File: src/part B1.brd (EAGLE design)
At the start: 41 x 75.5 mm, 0 parts

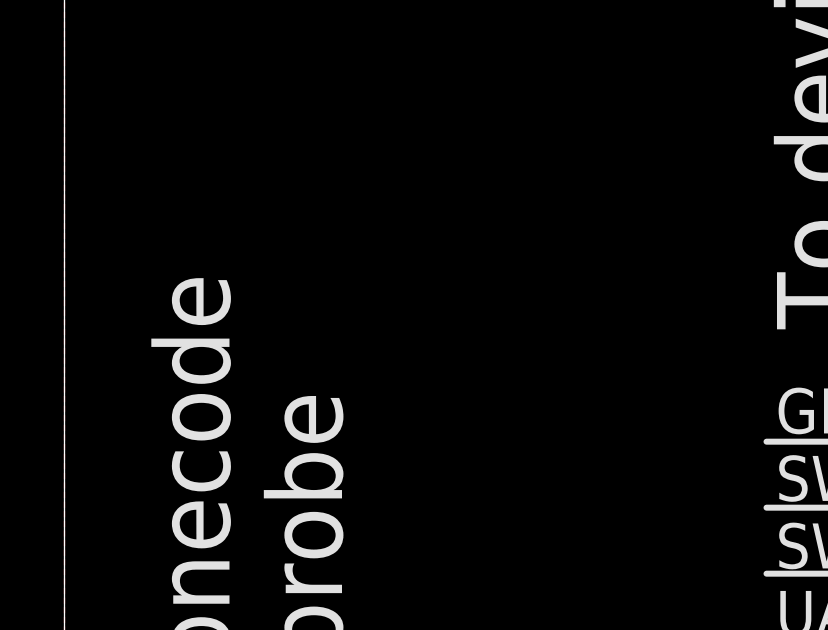
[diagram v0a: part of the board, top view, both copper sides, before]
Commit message: Fixed mosfet Q2 from both babel, fixes #6 (#12)
* removed mosfet Q2 from both babel, fixes #6

* removed Q2

* minor routing improvement

* cutout for DCP LED

* fixes #6

* trace width fixes #6

* ratnest fix, clean DRC
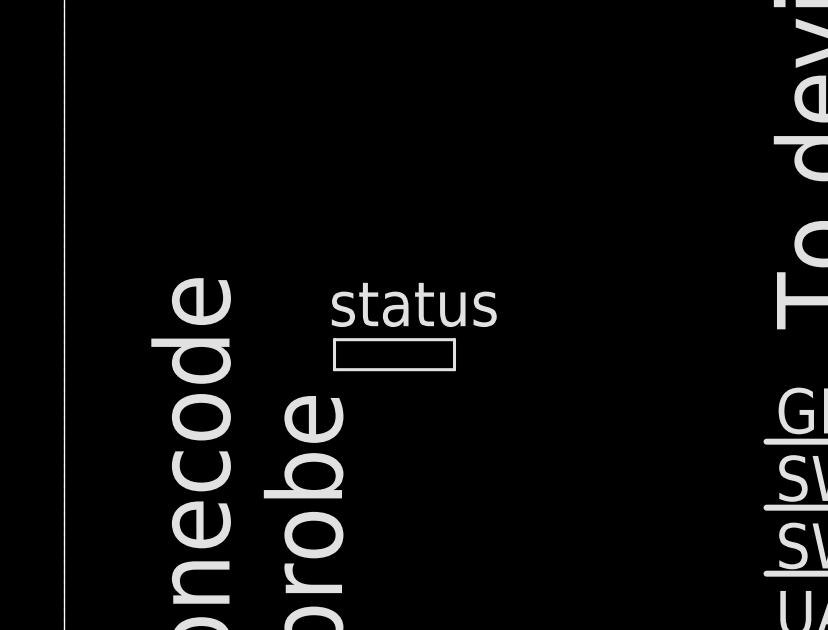
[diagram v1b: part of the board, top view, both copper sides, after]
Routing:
- added copper zone on layer 1, net S$7
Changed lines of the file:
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@@
 <layer number="28" name="bValues" color="7" fill="1" visible="yes" active="yes"/>
 <layer number="29" name="tStop" color="7" fill="3" visible="yes" active="yes"/>
-<layer number="30" name="bStop" color="7" fill="6" visible="no" active="yes"/>
+<layer number="30" name="bStop" color="7" fill="6" visible="yes" active="yes"/>
 <layer number="31" name="tCream" color="7" fill="4" visible="yes" active="yes"/>
 <layer number="32" name="bCream" color="7" fill="5" visible="yes" active="yes"/>
@@
 </layers>
 <board>
-<fusionsync huburn="a.cGVyc29uYWw6dWUyYWE4ZDY4" projecturn="a.cGVyc29uYWw6dWUyYWE4ZDY4IzIwMTgxMTAxMTU3ODkyNjgx" f3durn="urn:adsk.wipprod:dm.lineage:C2hCNDEwRimP04MRQMDYDQ" pcbguid="" lastpulledtime="" lastsyncedchangeguid="" latestrevisionid="0cd668d3-4819-4b12-b1bd-3aef8fff70f7" lastsyncedrevisionid="0cd668d3-4819-4b12-b1bd-3aef8fff70f7" lastboardhashguid="bda82eaa-9f63-2a0b-8d95-856cf3c33b22" lastpushedtime="2021-01-08T07:50:45Z" linktopcb3d="true"/>
+<fusionsync huburn="a.cGVyc29uYWw6dWUyYWE4ZDY4" projecturn="a.cGVyc29uYWw6dWUyYWE4ZDY4IzIwMTgxMTAxMTU3ODkyNjgx" f3durn="urn:adsk.wipprod:dm.lineage:C2hCNDEwRimP04MRQMDYDQ" pcbguid="" lastpulledtime="" lastsyncedchangeguid="" latestrevisionid="0cd668d3-4819-4b12-b1bd-3aef8fff70f7" lastsyncedrevisionid="0cd668d3-4819-4b12-b1bd-3aef8fff70f7" lastboardhashguid="bda82eaa-9f63-2a0b-8d95-856cf3c33b22" lastpushedtime="2021-01-08T07:50:45Z" linktopcb3d="false"/>
 <plain>
 <hole x="-2" y="69.5" drill="2"/>
@@
 <vertex x="28.2" y="3.4"/>
 <vertex x="28.2" y="4.4"/>
+</polygon>
+<wire x1="5" y1="51.2" x2="9" y2="51.2" width="0.1016" layer="21"/>
+<wire x1="9" y1="51.2" x2="9" y2="50.2" width="0.1016" layer="21"/>
+<wire x1="9" y1="50.2" x2="5" y2="50.2" width="0.1016" layer="21"/>
+<wire x1="5" y1="50.2" x2="5" y2="51.2" width="0.1016" layer="21"/>
+<text x="10.5" y="52.4" size="1.5" layer="21" font="vector" ratio="15" align="center-right">status</text>
+<polygon width="0.1" layer="30">
+<vertex x="5" y="51.2"/>
+<vertex x="9" y="51.2"/>
+<vertex x="9" y="50.2"/>
+<vertex x="5" y="50.2"/>
+</polygon>
+<polygon width="0.1" layer="29">
+<vertex x="5" y="51.2"/>
+<vertex x="9" y="51.2"/>
+<vertex x="9" y="50.2"/>
+<vertex x="5" y="50.2"/>
 </polygon>
 </plain>
@@
 </polygon>
 </signal>
+<signal name="S$7">
+<polygon width="0.1" layer="1" pour="cutout">
+<vertex x="5" y="51.2"/>
+<vertex x="9" y="51.2"/>
+<vertex x="9" y="50.2"/>
+<vertex x="5" y="50.2"/>
+</polygon>
+</signal>
